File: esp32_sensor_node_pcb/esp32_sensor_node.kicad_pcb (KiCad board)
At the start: 2 copper layers, 56.9 x 60.5 mm, 17 parts, among them SW1 SW_DIP_x01, U1 ESP32-WROOM-E, U2 AP2127R-3.3, U3 MAX3483AEASA+

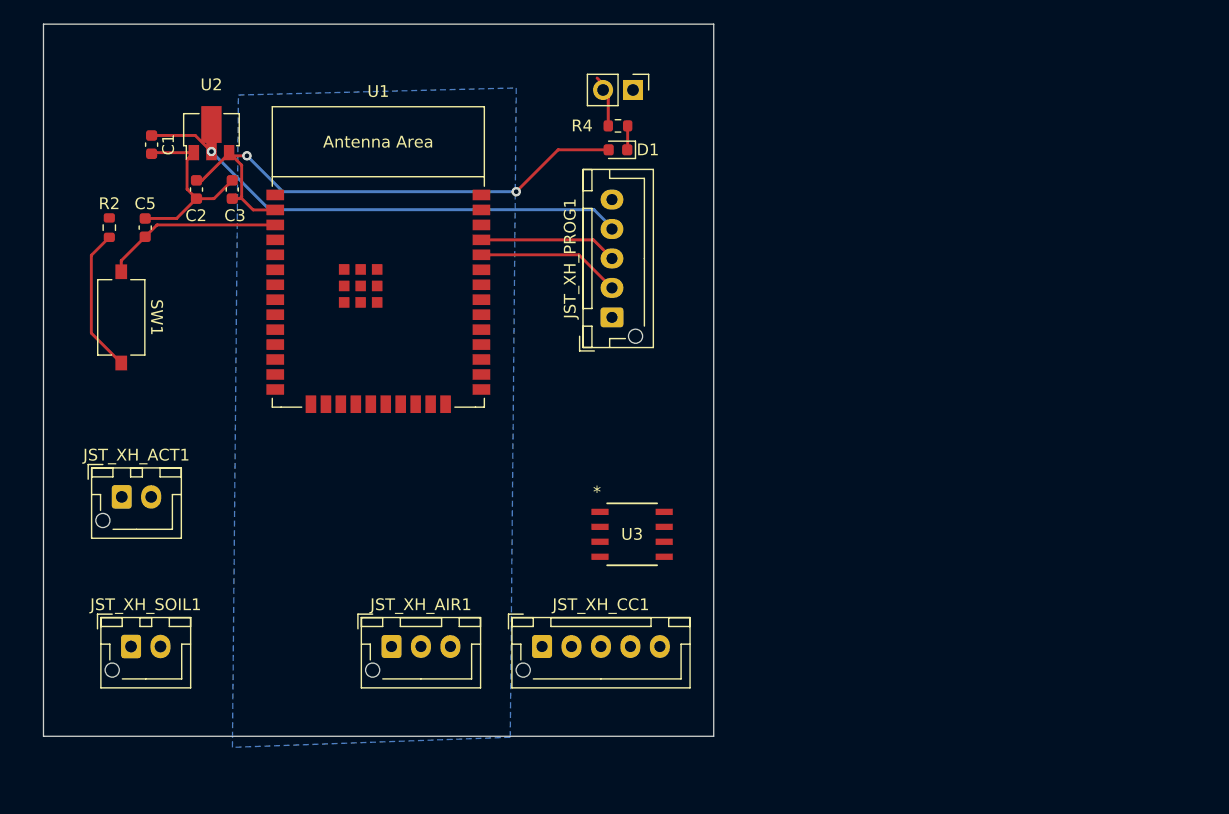
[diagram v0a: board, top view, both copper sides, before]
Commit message: Added big 0805 22u capacitor, fixed reset capacitor, add capacitor for max ic decoupling
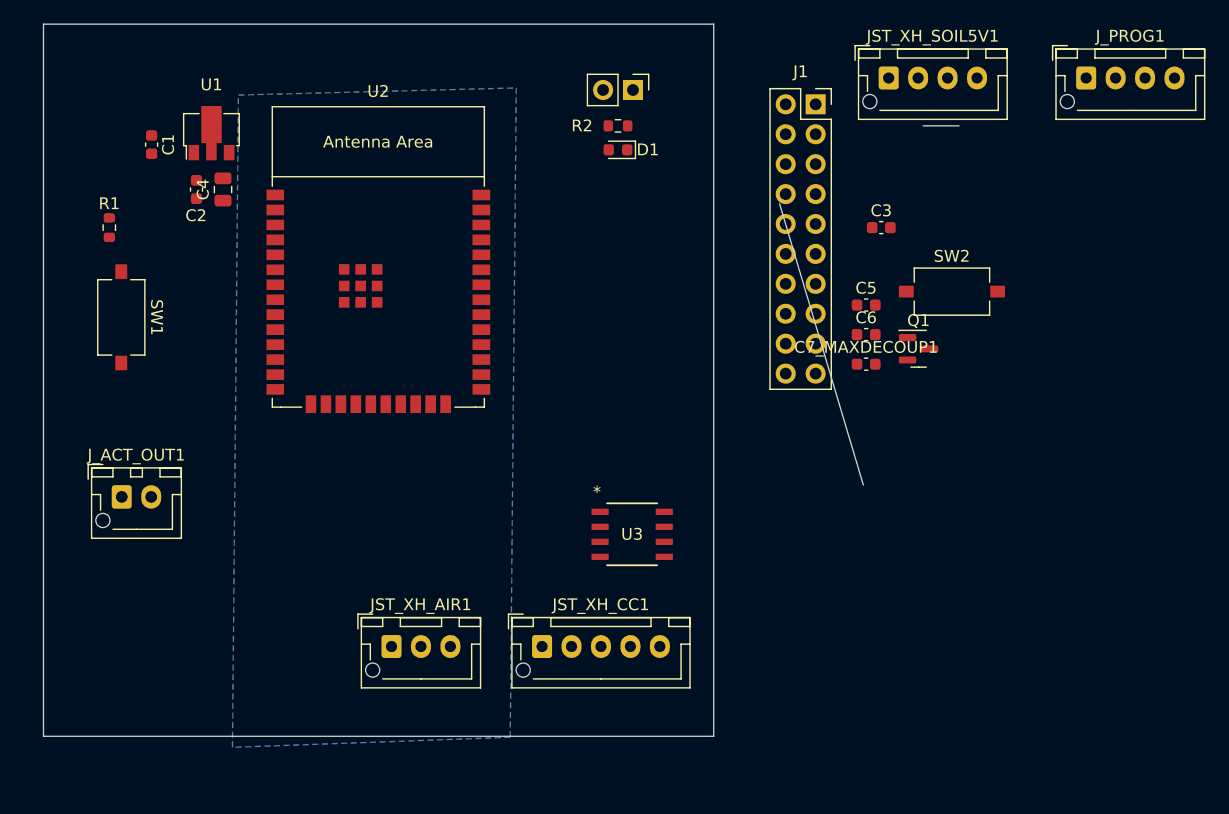
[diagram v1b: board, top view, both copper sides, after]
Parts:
- removed JST_XH_PROG1: Conn_01x05_Socket, Connector_JST:JST_XH_B5B-XH-AM_1x05_P2.50mm_Vertical
- removed JST_XH_SOIL1: Conn_01x02_Socket, Connector_JST:JST_XH_B2B-XH-AM_1x02_P2.50mm_Vertical
- added C3: 0.1uF, Capacitor_SMD:C_0603_1608Metric, F.Cu at (92.5, 33.0)
- added C6: 0.1uF, Capacitor_SMD:C_0603_1608Metric, F.Cu at (91.2, 42.1)
- added C7_MAXDECOUP1: 0.1uF, Capacitor_SMD:C_0603_1608Metric, F.Cu at (91.2, 44.6)
- added J1: Conn_02x10_Top_Bottom, Connector_PinSocket_2.54mm:PinSocket_2x10_P2.54mm_Vertical, F.Cu at (86.9, 22.6)
- added JST_XH_SOIL5V1: Conn_01x04_Socket, Connector_JST:JST_XH_B4B-XH-AM_1x04_P2.50mm_Vertical, F.Cu at (93.1, 20.3)
- added J_PROG1: Conn_01x04_Socket, Connector_JST:JST_XH_B4B-XH-AM_1x04_P2.50mm_Vertical, F.Cu at (109.8, 20.3)
- added Q1: 2N7002K, Package_TO_SOT_SMD:SOT-23, F.Cu at (95.6, 43.3)
- added SW2: SW_DIP_x01, Button_Switch_SMD:SW_Tactile_SPST_NO_Straight_CK_PTS636Sx25SMTRLFS, F.Cu at (98.5, 38.5)
- C4: renamed from C3; footprint Capacitor_SMD:C_0603_1608Metric -> Capacitor_SMD:C_0805_2012Metric
- R2: renamed from R4; value 500R -> 1.91K
- U1: renamed from U2; value AP2127R-3.3 -> HT7833
- moved C5 61.6 mm to (91.2, 39.6), turned to 0 degrees
- moved C4 0.78 mm to (36.6, 29.8)
- renumbered JST_XH_ACT1 to J_ACT_OUT1, R2 to R1, U1 to U2
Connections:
- net GPIO15 renamed RS485_*RE
- C1 pad 1: 5V -> +5V
- C2 pad 1: 3V3 -> +3.3V
- C4 pad 1: 3V3 -> +3.3V
- D1 pad 2: 3V3 -> +3.3V
- JST_XH_AIR1 pad 1: Net-(JST_XH_AIR1-Pin_1) -> +3.3V
- JST_XH_AIR1 pad 2: 3V3 -> Net-(JST_XH_AIR1-Pin_2)
- J_ACT_OUT1 pad 1: Net-(JST_XH_ACT1-Pin_1) -> Net-(J_ACT_OUT1-Pin_1)
- R1 pad 1: 3V3 -> +3.3V
- R1 pad 2: Net-(R2-Pad2) -> RESET
- SW1 pad 1: RESET -> GND
- SW1 pad 2: Net-(R2-Pad2) -> RESET
- U1 pad 2: 5V -> +5V
- U1 pad 3: 3V3 -> +3.3V
- U2 pad 10: unconnected-(U1-DAC_1/ADC2_CH8/GPIO25-Pad10) -> SENSOR_EN
- U2 pad 11: unconnected-(U1-DAC_2/ADC2_CH9/GPIO26-Pad11) -> GPIO26
- U2 pad 16: unconnected-(U1-MTCK/GPIO13/ADC2_CH4-Pad16) -> GPIO13
- U2 pad 2: 3V3 -> +3.3V
- U2 pad 24: unconnected-(U1-ADC2_CH2/GPIO2-Pad24) -> GPIO2_DONT_USE
- U2 pad 30: unconnected-(U1-GPIO18-Pad30) -> GPIO18
- U2 pad 31: unconnected-(U1-GPIO19-Pad31) -> GPIO19
- U2 pad 33: unconnected-(U1-GPIO21-Pad33) -> GPIO21
- U2 pad 36: Net-(JST_XH_AIR1-Pin_1) -> Net-(JST_XH_AIR1-Pin_2)
- U2 pad 37: unconnected-(U1-GPIO23-Pad37) -> GPIO23
- U2 pad 4: unconnected-(U1-SENSOR_VP/GPIO36/ADC1_CH0-Pad4) -> GPIO36
- U2 pad 5: unconnected-(U1-SENSOR_VN/GPIO39/ADC1_CH3-Pad5) -> GPIO39
- U2 pad 6: unconnected-(U1-GPIO34/ADC1_CH6-Pad6) -> GPIO34
- U2 pad 7: unconnected-(U1-GPIO35/ADC1_CH7-Pad7) -> GPIO35
- U2 pad 8: ACT_OUT -> Net-(J_ACT_OUT1-Pin_1)
- U2 pad 9: Net-(JST_XH_ACT1-Pin_1) -> ACT_IN
- U3 pad 8: 5V -> +3.3V
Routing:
- net 3V3: track 47.8 -> 0.00 mm, vias 2 -> 0
- net 5V: track 42.4 -> 0.00 mm, vias 1 -> 0
- net GND: track 17.2 -> 0.00 mm
- net RESET: track 15.3 -> 0.00 mm
- net Net-(R2-Pad2): track 12.4 -> 0.00 mm
- net Net-(J_PROG1-Pin_1): track 12.2 -> 0.00 mm
- net Net-(J_PROG1-Pin_2): track 11.7 -> 0.00 mm
- net Net-(JP1-B): track 4.46 -> 0.00 mm
- net Net-(D1-K): track 2.05 -> 0.00 mm
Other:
- board size 56.9 x 60.5 mm -> 77.7 x 60.5 mm

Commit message: Add mounting holes
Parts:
- added H1: MountingHole_Pad, MountingHole:MountingHole_3.2mm_M3, F.Cu at (35.1, 37.1)
- added H2: MountingHole_Pad, MountingHole:MountingHole_3.2mm_M3, F.Cu at (35.1, 45.1)
- added H3: MountingHole_Pad, MountingHole:MountingHole_3.2mm_M3, F.Cu at (35.1, 53.0)
- added H4: MountingHole_Pad, MountingHole:MountingHole_3.2mm_M3, F.Cu at (35.1, 61.0)
- moved J_ACT_OUT1 14.2 mm to (27.9, 70.1)
- moved J1 8.15 mm to (79.2, 25.4)
- moved U3 4.19 mm to (68.1, 56.4)
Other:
- board size 77.7 x 60.5 mm -> 77.7 x 56.8 mm
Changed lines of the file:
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@@
     )
+  )
+  (footprint "MountingHole:MountingHole_3.2mm_M3" (layer "F.Cu")
+    (at 35.052 53.01)
+    (descr "Mounting Hole 3.2mm, no annular, M3")
+    (tags "mounting hole 3.2mm no annular m3")
+    (property "Sheetfile" "esp32_sensor_node.kicad_sch")
+    (property "Sheetname" "")
+    (property "ki_description" "Mounting Hole with connection")
+    (property "ki_keywords" "mounting hole")
+    (attr exclude_from_pos_files)
+    (fp_text reference "H3" (at 0 -4.2) (layer "F.SilkS")
+        (effects (font (size 1 1) (thickness 0.15)))
+    )
+    (fp_text value "MountingHole_Pad" (at 0 4.2) (layer "F.Fab")
+        (effects (font (size 1 1) (thickness 0.15)))
+    )
+    (fp_text user "${REFERENCE}" (at 0 0) (layer "F.Fab")
+        (effects (font (size 1 1) (thickness 0.15)))
+    )
+    (fp_circle (center 0 0) (end 3.2 0)
+      (stroke (width 0.15) (type solid)) (fill none) (layer "Cmts.User"))
+    (fp_circle (center 0 0) (end 3.45 0)
+      (stroke (width 0.05) (type solid)) (fill none) (layer "F.CrtYd"))
+    (pad "" np_thru_hole circle (at 0 0) (size 3.2 3.2) (drill 3.2) (layers "*.Cu" "*.Mask"))
   )
   (footprint "Capacitor_SMD:C_0603_1608Metric" (layer "F.Cu")
@@
       (rotate (xyz 0 0 0))
     )
+  )
+  (footprint "MountingHole:MountingHole_3.2mm_M3" (layer "F.Cu")
+    (at 35.052 37.11)
+    (descr "Mounting Hole 3.2mm, no annular, M3")
+    (tags "mounting hole 3.2mm no annular m3")
+    (property "Sheetfile" "esp32_sensor_node.kicad_sch")
+    (property "Sheetname" "")
+    (property "ki_description" "Mounting Hole with connection")
+    (property "ki_keywords" "mounting hole")
+    (attr exclude_from_pos_files)
+    (fp_text reference "H1" (at 0 -4.2) (layer "F.SilkS")
+        (effects (font (size 1 1) (thickness 0.15)))
+    )
+    (fp_text value "MountingHole_Pad" (at 0 4.2) (layer "F.Fab")
+        (effects (font (size 1 1) (thickness 0.15)))
+    )
+    (fp_text user "${REFERENCE}" (at 0 0) (layer "F.Fab")
+        (effects (font (size 1 1) (thickness 0.15)))
+    )
+    (fp_circle (center 0 0) (end 3.2 0)
+      (stroke (width 0.15) (type solid)) (fill none) (layer "Cmts.User"))
+    (fp_circle (center 0 0) (end 3.45 0)
+      (stroke (width 0.05) (type solid)) (fill none) (layer "F.CrtYd"))
+    (pad "" np_thru_hole circle (at 0 0) (size 3.2 3.2) (drill 3.2) (layers "*.Cu" "*.Mask"))
   )
   (footprint "Package_TO_SOT_SMD:SOT-89-3" (layer "F.Cu")
@@
     )
   )
+  (footprint "MountingHole:MountingHole_3.2mm_M3" (layer "F.Cu")
+    (at 35.052 60.96)
+    (descr "Mounting Hole 3.2mm, no annular, M3")
+    (tags "mounting hole 3.2mm no annular m3")
+    (property "Sheetfile" "esp32_sensor_node.kicad_sch")
+    (property "Sheetname" "")
+    (property "ki_description" "Mounting Hole with connection")
+    (property "ki_keywords" "mounting hole")
+    (attr exclude_from_pos_files)
+    (fp_text reference "H4" (at 0 -4.2) (layer "F.SilkS")
+        (effects (font (size 1 1) (thickness 0.15)))
+    )
+    (fp_text value "MountingHole_Pad" (at 0 4.2) (layer "F.Fab")
+        (effects (font (size 1 1) (thickness 0.15)))
+    )
+    (fp_text user "${REFERENCE}" (at 0 0) (layer "F.Fab")
+        (effects (font (size 1 1) (thickness 0.15)))
+    )
+    (fp_circle (center 0 0) (end 3.2 0)
+      (stroke (width 0.15) (type solid)) (fill none) (layer "Cmts.User"))
+    (fp_circle (center 0 0) (end 3.45 0)
+      (stroke (width 0.05) (type solid)) (fill none) (layer "F.CrtYd"))
+    (pad "" np_thru_hole circle (at 0 0) (size 3.2 3.2) (drill 3.2) (layers "*.Cu" "*.Mask"))
+  )
   (footprint "Connector_JST:JST_XH_B4B-XH-AM_1x04_P2.50mm_Vertical" (layer "F.Cu")
     (at 93.084 20.32)
@@
     )
   )
+  (footprint "MountingHole:MountingHole_3.2mm_M3" (layer "F.Cu")
+    (at 35.052 45.06)
+    (descr "Mounting Hole 3.2mm, no annular, M3")
+    (tags "mounting hole 3.2mm no annular m3")
+    (property "Sheetfile" "esp32_sensor_node.kicad_sch")
+    (property "Sheetname" "")
+    (property "ki_description" "Mounting Hole with connection")
+    (property "ki_keywords" "mounting hole")
+    (attr exclude_from_pos_files)
+    (fp_text reference "H2" (at 0 -4.2) (layer "F.SilkS")
+        (effects (font (size 1 1) (thickness 0.15)))
+    )
+    (fp_text value "MountingHole_Pad" (at 0 4.2) (layer "F.Fab")
+        (effects (font (size 1 1) (thickness 0.15)))
+    )
+    (fp_text user "${REFERENCE}" (at 0 0) (layer "F.Fab")
+        (effects (font (size 1 1) (thickness 0.15)))
+    )
+    (fp_circle (center 0 0) (end 3.2 0)
+      (stroke (width 0.15) (type solid)) (fill none) (layer "Cmts.User"))
+    (fp_circle (center 0 0) (end 3.45 0)
+      (stroke (width 0.05) (type solid)) (fill none) (layer "F.CrtYd"))
+    (pad "" np_thru_hole circle (at 0 0) (size 3.2 3.2) (drill 3.2) (layers "*.Cu" "*.Mask"))
+  )
   (footprint "Capacitor_SMD:C_0805_2012Metric" (layer "F.Cu")
     (at 36.576 29.785 90)
@@
   )
   (footprint "Connector_PinSocket_2.54mm:PinSocket_2x10_P2.54mm_Vertical" (layer "F.Cu")
-    (at 86.883 22.554)
+    (at 79.248 25.4)
     (descr "Through hole straight socket strip, 2x10, 2.54mm pitch, double cols (from Kicad 4.0.7), script generated")
     (tags "Through hole socket strip THT 2x10 2.54mm double row")
@@
   )
   (footprint "Connector_JST:JST_XH_B2B-XH-AM_1x02_P2.50mm_Vertical" (layer "F.Cu")
-    (at 27.98 55.88)
+    (at 27.94 70.104)
     (descr "JST XH series connector, B2B-XH-AM, with boss (http://www.jst-mfg.com/product/pdf/eng/eXH.pdf), generated with kicad-footprint-generator")
     (tags "connector JST XH vertical boss")
@@
   )
   (footprint "MAX3483:21-0041B_8_MXM" (layer "F.Cu")
-    (at 71.30415 59.055)
+    (at 68.072 56.388)
     (tags "MAX3483AEASA+ ")
     (property "Sheetfile" "esp32_sensor_node.kicad_sch")
@@
   (gr_line (start 96.012 24.384) (end 99.06 24.384)
     (stroke (width 0.1) (type default)) (layer "Edge.Cuts"))
-  (gr_rect (start 21.336 15.748) (end 78.232 76.2)
+  (gr_rect (start 21.336 15.748) (end 78.232 72.551168)
     (stroke (width 0.1) (type default)) (fill none) (layer "Edge.Cuts"))
   (gr_line (start 90.932 54.864) (end 83.82 30.988)

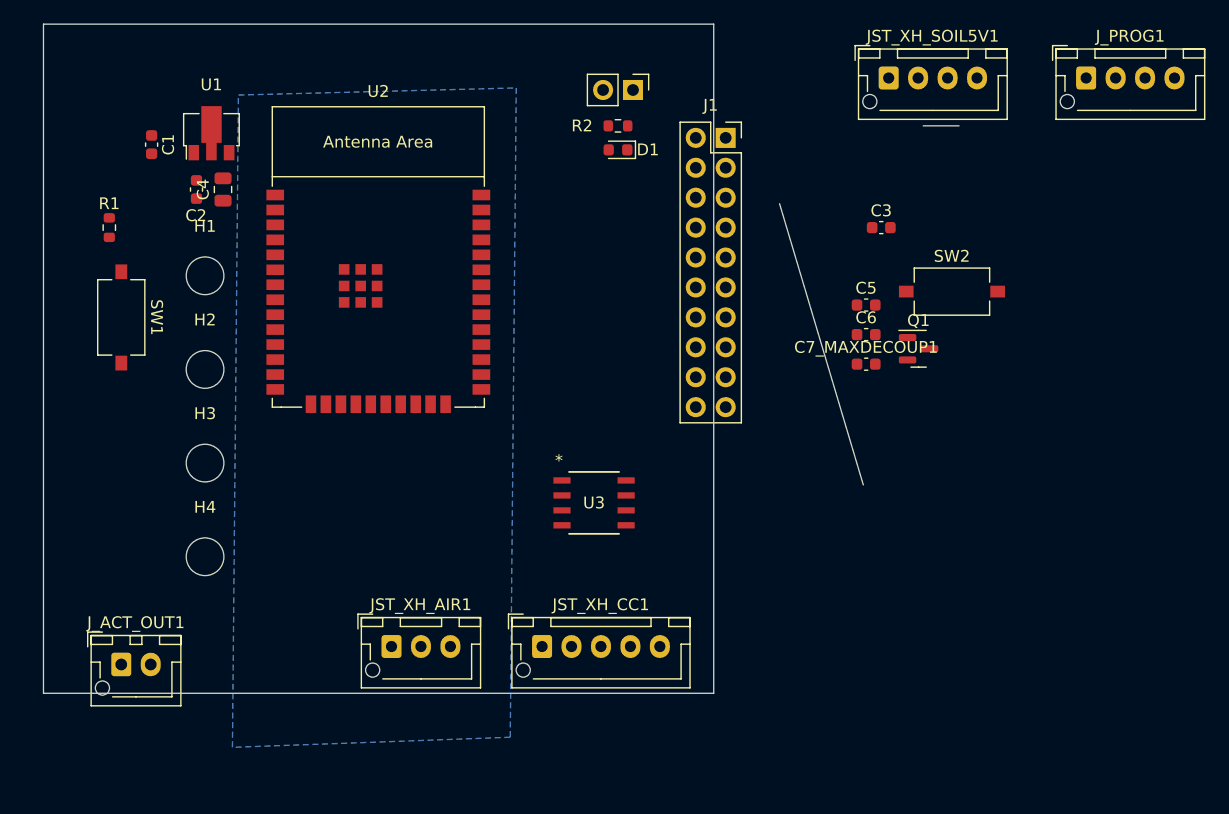
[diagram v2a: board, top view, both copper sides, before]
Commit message: Setup initial board layout
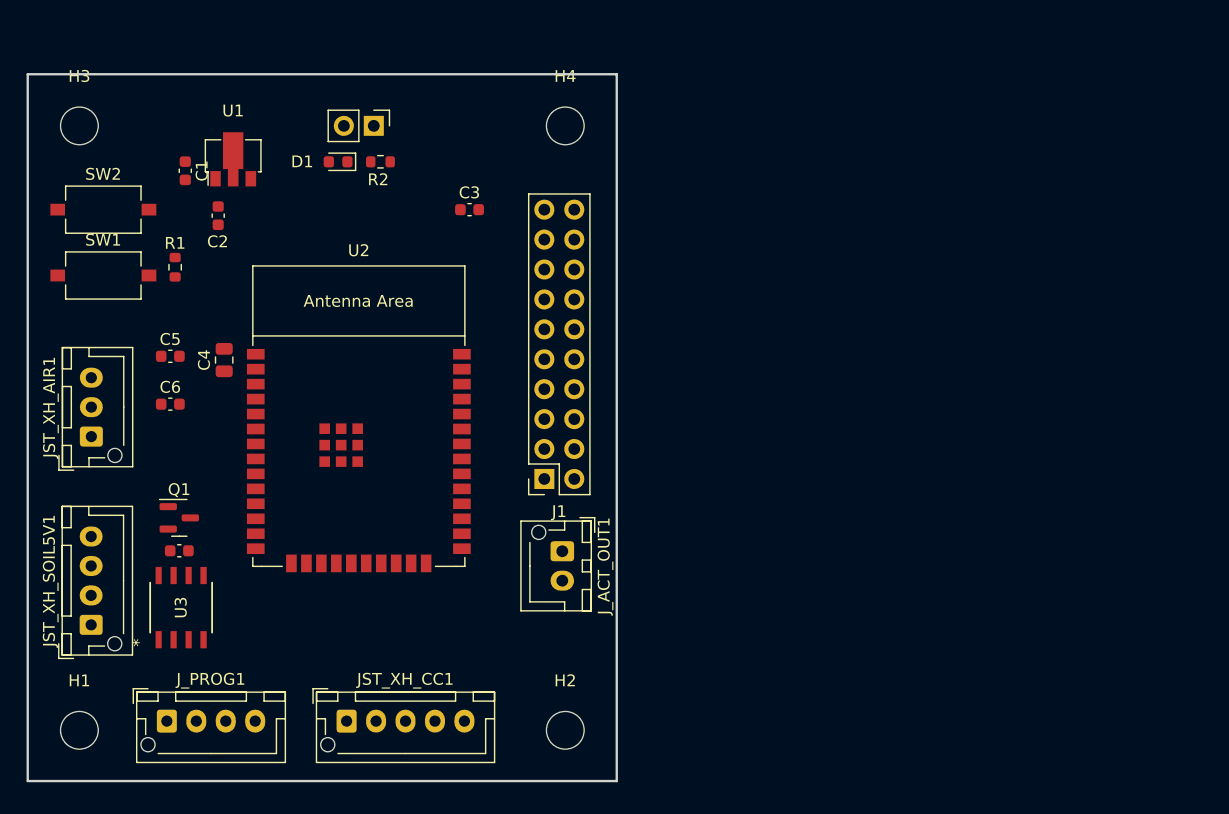
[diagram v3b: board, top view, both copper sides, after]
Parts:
- H1, H2, H3, H4: value MountingHole_Pad -> MountingHole
- moved J_PROG1 95.2 mm to (31.8, 74.9)
- moved JST_XH_SOIL5V1 82.1 mm to (25.4, 66.7), turned to 90 degrees
- moved SW2 72.4 mm to (26.4, 31.5)
- moved Q1 64.4 mm to (32.9, 57.7)
- moved C7_MAXDECOUP1 60.4 mm to (32.9, 60.5), turned to 180 degrees
- moved C6 59.4 mm to (32.1, 48.0)
- moved C5 59.2 mm to (32.1, 43.9)
- moved H4 47.7 mm to (65.6, 24.4)
- moved H2 43.3 mm to (65.6, 75.7)
- moved H1 40.0 mm to (24.4, 75.7)
- moved J_ACT_OUT1 38.7 mm to (65.4, 60.5), turned to -90 degrees
- moved U3 36.2 mm to (33.0, 65.3), turned to 90 degrees
- moved C3 35.0 mm to (57.5, 31.5)
- moved J1 32.8 mm to (63.9, 54.4), turned to 180 degrees
- moved JST_XH_AIR1 31.1 mm to (25.4, 50.8), turned to 90 degrees
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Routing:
- removed copper zone on B.Cu, net GND
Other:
- board size 77.7 x 56.8 mm -> 50 x 60 mm
